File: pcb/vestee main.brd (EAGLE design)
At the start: 65 x 65 mm, 45 parts, among them IC1 LD117AS12TR, IC2 FT232RL, Q1 MMBT2222A, Q3 MMBT4403

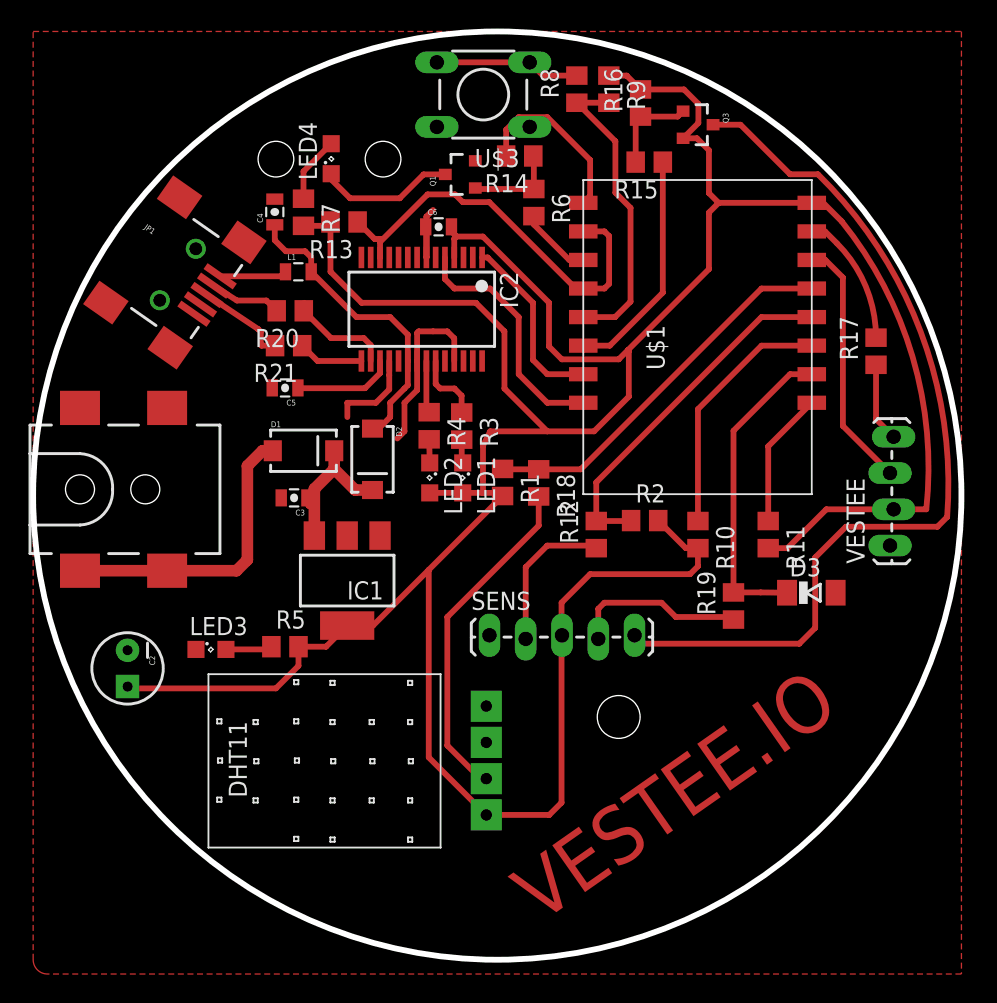
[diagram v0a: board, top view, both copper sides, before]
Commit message: Fixed discovered issues, removed DC jack, added jack for 1-Wire, minor improvements
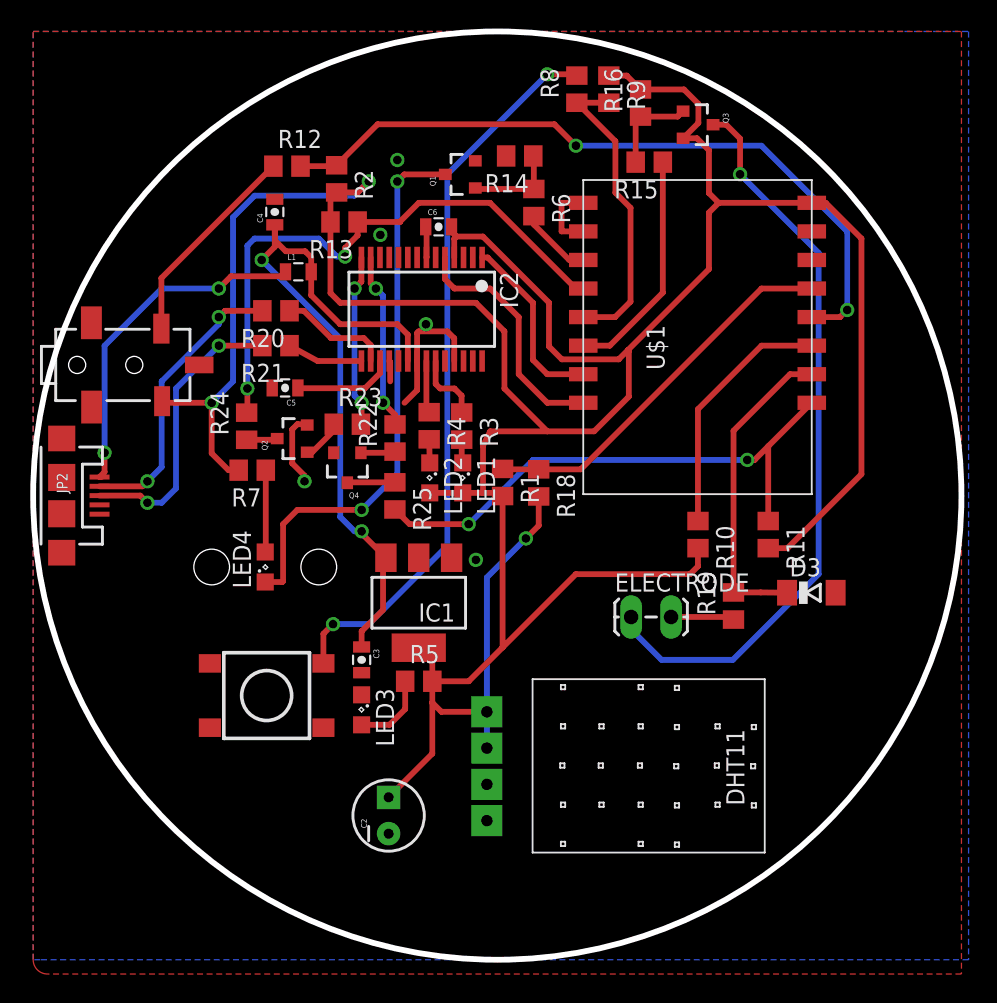
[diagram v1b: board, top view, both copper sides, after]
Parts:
- removed D1, D2: (no value), SparkFun-DiscreteSemi:SMA-DIODE
- removed JP1: USB-SMD-NS, SparkFun-Connectors:USB-MINIB-NOSTOP
- removed R17: (no value), rcl:R0805
- removed SENS: (no value), SparkFun-Connectors:1X05_LOCK_LONGPADS
- removed U$3: TACTILE-SWITCH-PTH, GeekAmmo:TAC-SWITCH-PTH
- removed VESTEE: (no value), SparkFun-Connectors:1X04_LOCK_LONGPADS
- added ELECTRODE: (no value), SparkFun-Connectors:1X02_LOCK_LONGPADS
- added PRPIHERALS: (no value), SparkFun-Connectors:STEREOJACK2.5MM
- added Q2, Q4: MMBT5088, SparkFun-DiscreteSemi:SOT23-3
- added R22, R23, R24, R25: (no value), rcl:R0805
- added S2: SWITCH-MOMENTARY-2SMD-4, SparkFun-Electromechanical:TACTILE_SWITCH_TALL
- JP2: value 5.5x2.1mm Barrel -> USB-MICROB; device SparkFun-Connectors:POWER_JACK_SMD -> SparkFun-Connectors:USB-MICROB
- moved R12 33.7 mm to (17.8, 55.6), turned to 0 degrees
- moved R2 32.2 mm to (21.2, 54.7), turned to 270 degrees
- moved LED4 29.0 mm to (16.2, 27.5)
- moved U$2 22.9 mm to (43.2, 13.6), turned to 270 degrees
- moved C2 21.0 mm to (24.9, 10.1), turned to 90 degrees
- moved R7 18.4 mm to (15.3, 34.3), turned to 180 degrees
- moved C3 12.3 mm to (23.0, 21.0), turned to 270 degrees
- moved LED3 11.4 mm to (23.0, 17.5), turned to 270 degrees
- moved R5 9.68 mm to (27.0, 19.5)
- moved IC1 5.24 mm to (27.0, 25.0)
- moved JP2 1.35 mm to (2.00, 32.5), turned to 270 degrees
- moved R20 1.00 mm to (17.0, 45.4)
- moved R21 0.89 mm to (17.0, 43.0)
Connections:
- removed net FLOW: R17.2, U$1.GPIO13
- removed net N$20: R12.1, SENS.2
- removed net N$22: R11.1, U$1.REST
- removed net N$23: C4.1, D2.A, IC2.20, L1.2
- removed net N$24: U$1.GPIO12, VESTEE.3
- removed net N$25: Q3.3, SENS.5
- removed net N$5: R17.1, VESTEE.4
- new net 1-WIRE: PRPIHERALS.1, R12.1
- new net CBUS_RST: R11.1, R25.2, U$1.REST
- new net N$30: IC2.13, R22.2
- new net N$31: Q2.3, R24.1
- new net N$32: Q2.1, R23.1
- new net N$33: Q4.1, R22.1
- new net N$34: IC2.14, R23.2
- new net N$35: Q4.3, R25.1
- net CBUS: now also R24.2; no longer IC2.12, U$1.GPIO15
- net GND: now also IC2.26, JP2.GND, JP2.MT1, JP2.MT2, PRPIHERALS.5, Q2.2, Q4.2, S2.A2, U$1.GPIO15; no longer JP1.GND, JP2.VIN0, SENS.1, U$3.1, U$3.2, VESTEE.1
- net N$17: now also ELECTRODE.1, Q3.3; no longer D1.A, JP2.GND, JP2.P$4
- net N$18: now also S2.B2; no longer U$3.3, U$3.4
- net N$2: now also JP2.D+; no longer JP1.D+
- net N$26: now also ELECTRODE.2; no longer SENS.4
- net N$3: now also JP2.D-; no longer JP1.D-
- net N$7: now also JP2.VBUS; no longer JP1.VBUS
- net VCC: now also PRPIHERALS.4; no longer SENS.3, VESTEE.2
- net VIN: now also C4.1, IC2.20, L1.2; no longer D1.C, D2.C
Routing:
- net N$25: track 63.1 -> 0.00 mm
- net N$18: track 10.2 -> 51.3 mm, vias 0 -> 2
- net VIN: track 11.4 -> 51.1 mm, vias 0 -> 2
- net CBUS_RST: track 0.00 -> 38.4 mm, vias 0 -> 2
- net N$17: track 20.8 -> 52.4 mm, vias 0 -> 1
- net N$16: track 9.63 -> 38.8 mm, vias 0 -> 2
- net N$4: track 25.0 -> 50.8 mm, vias 0 -> 2
- net N$23: track 21.6 -> 0.00 mm
- net N$7: track 4.70 -> 24.3 mm, vias 0 -> 2
- net N$24: track 17.7 -> 0.00 mm
- net N$3: track 5.02 -> 20.3 mm, vias 0 -> 2
- net 1-WIRE: track 0.00 -> 14.6 mm
- net N$2: track 6.51 -> 20.3 mm, vias 0 -> 2
- net GND: track 37.0 -> 23.6 mm, vias 0 -> 5
- net N$30: track 0.00 -> 12.4 mm, vias 0 -> 2
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- added copper zone on layer 16, net GND
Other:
- board text removed: "VESTEE.IO"

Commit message: Fixed silkscreen
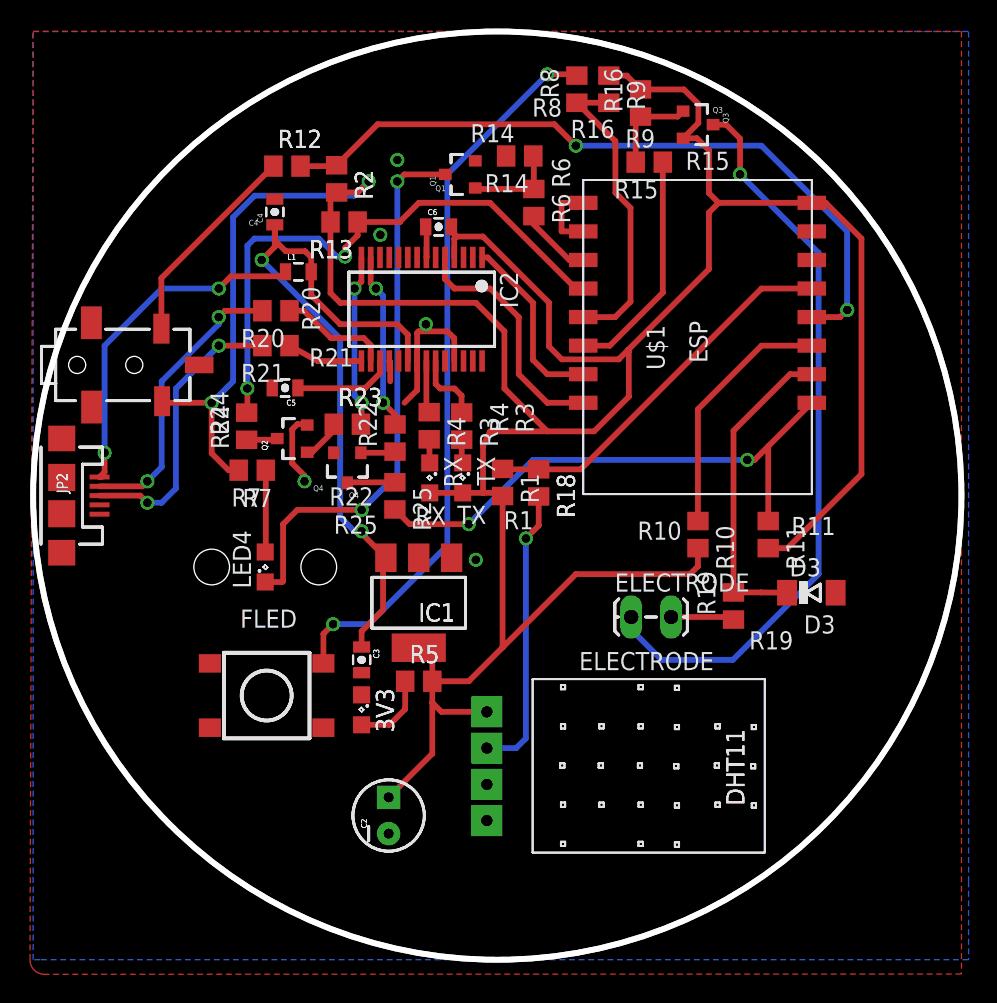
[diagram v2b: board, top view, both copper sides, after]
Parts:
- renumbered LED1 to TX, LED2 to RX, LED3 to 3V3
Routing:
- net N$6: track 19.1 -> 20.3 mm
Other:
- board text added: "/Users/grzegorz/Documents/montebmp.bmp"
- board text added: "3V3"
- board text added: "C2"
- board text added: "C3"
- board text added: "C4"
- board text added: "C5"
- board text added: "C6"
- board text added: "D3"
- board text added: "DHT11"
- board text added: "ELECTRODE"
- board text added: "ESP"
- board text added: "FLED"
- board text added: "IC1"
- board text added: "JP2"
- board text added: "L1"
- board text added: "Q1"
- board text added: "Q2"
- board text added: "Q3"
- board text added: "Q4"
- board text added: "R1"
- board text added: "R10"
- board text added: "R11"
- board text added: "R12"
- board text added: "R13"
- board text added: "R14"
- board text added: "R15"
- board text added: "R16"
- board text added: "R18"
- board text added: "R19"
- board text added: "R2"
- board text added: "R20"
- board text added: "R21"
- board text added: "R22"
- board text added: "R23"
- board text added: "R24"
- board text added: "R25"
- board text added: "R3"
- board text added: "R4"
- board text added: "R5"
- board text added: "R6"
- board text added: "R7"
- board text added: "R8"
- board text added: "R9"
- board text added: "RX"
- board text added: "TX"
- board text added: "vestee"
- board text added: "vestee for Monterail"
